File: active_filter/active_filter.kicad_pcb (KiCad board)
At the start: 2 copper layers, 16 parts, among them J1 Screw_Terminal_01x03, J2 Screw_Terminal_01x02, U1 ADA4610-2

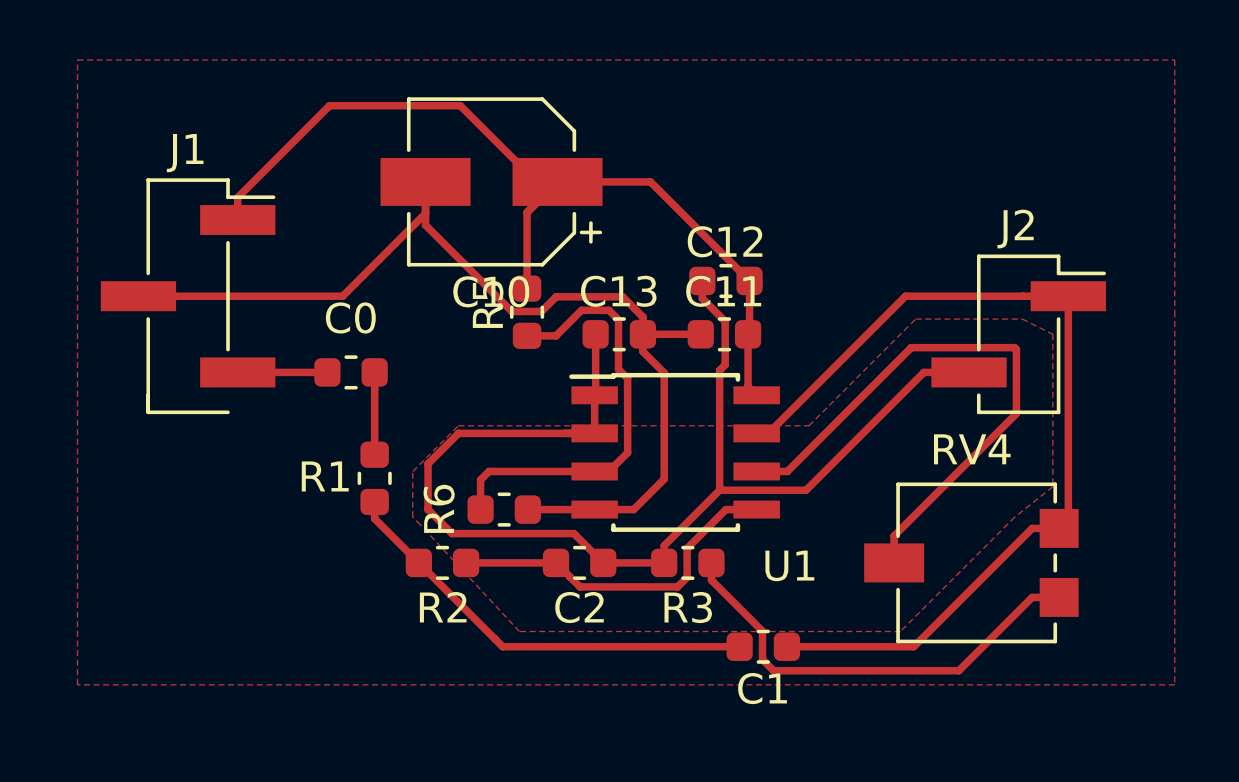
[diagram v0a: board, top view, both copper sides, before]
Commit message: shortened some traces
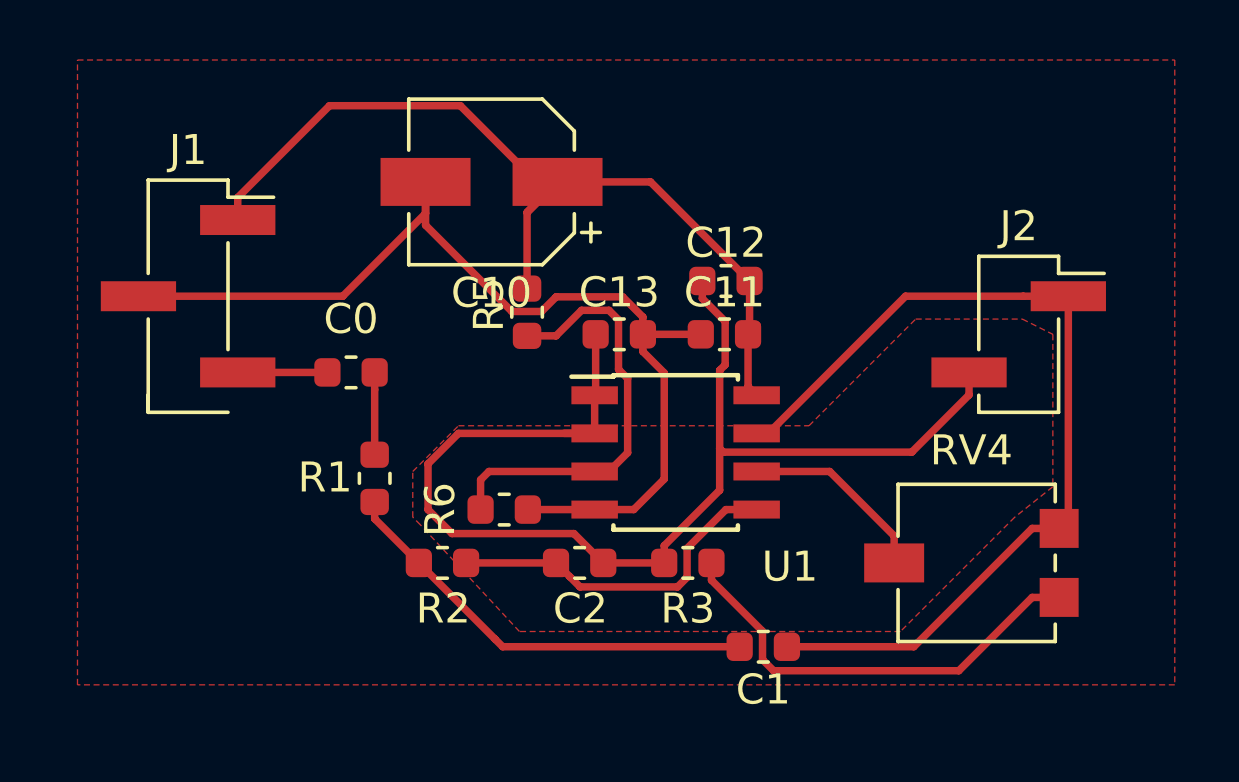
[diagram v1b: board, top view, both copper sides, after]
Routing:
- net Net-(RV4-Pad2): track 19.2 -> 6.37 mm
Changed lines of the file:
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@@
-(kicad_pcb (version 20171130) (host pcbnew 5.0.0)
+(kicad_pcb (version 20171130) (host pcbnew 5.0.0-fee4fd1~66~ubuntu16.04.1)
   (general
     (thickness 1.6)
     (drawings 0)
-    (tracks 107)
+    (tracks 105)
     (zones 0)
     (modules 16)
@@
   (segment (start 30.988 33.782) (end 35.527 33.782) (width 0.25) (layer F.Cu) (net 6))
   (segment (start 29.972 34.798) (end 30.988 33.782) (width 0.25) (layer F.Cu) (net 6))
-  (segment (start 46.501 31.75) (end 48.006 31.75) (width 0.25) (layer F.Cu) (net 6))
-  (segment (start 42.573999 35.677001) (end 46.501 31.75) (width 0.25) (layer F.Cu) (net 6))
-  (segment (start 39.693999 35.677001) (end 42.573999 35.677001) (width 0.25) (layer F.Cu) (net 6))
   (segment (start 37.846 37.525) (end 39.693999 35.677001) (width 0.25) (layer F.Cu) (net 6))
   (segment (start 37.846 38.1) (end 37.846 37.525) (width 0.25) (layer F.Cu) (net 6))
@@
   (segment (start 39.116 28.702) (end 39.116 29.287006) (width 0.25) (layer F.Cu) (net 6))
   (segment (start 39.116 29.287006) (end 39.87749 30.048496) (width 0.25) (layer F.Cu) (net 6))
-  (segment (start 39.693999 31.680001) (end 39.693999 35.677001) (width 0.25) (layer F.Cu) (net 6))
   (segment (start 39.87749 31.49651) (end 39.693999 31.680001) (width 0.25) (layer F.Cu) (net 6))
+  (segment (start 39.811 34.407001) (end 39.693999 34.29) (width 0.25) (layer F.Cu) (net 6))
+  (segment (start 48.006 32.5) (end 46.098999 34.407001) (width 0.25) (layer F.Cu) (net 6))
+  (segment (start 48.006 31.75) (end 48.006 32.5) (width 0.25) (layer F.Cu) (net 6))
+  (segment (start 39.693999 31.680001) (end 39.693999 34.29) (width 0.25) (layer F.Cu) (net 6))
+  (segment (start 46.098999 34.407001) (end 39.811 34.407001) (width 0.25) (layer F.Cu) (net 6))
+  (segment (start 39.693999 34.29) (end 39.693999 35.677001) (width 0.25) (layer F.Cu) (net 6))
   (segment (start 23.63 25.92) (end 26.69 22.86) (width 0.25) (layer F.Cu) (net 7))
   (segment (start 23.63 26.67) (end 23.63 25.92) (width 0.25) (layer F.Cu) (net 7))
@@
   (segment (start 37.135 30.48) (end 39.065 30.48) (width 0.25) (layer F.Cu) (net 8))
   (segment (start 36.002 36.322) (end 35.527 36.322) (width 0.25) (layer F.Cu) (net 8))
-  (segment (start 31.699 36.322) (end 31.496 36.119) (width 0.25) (layer F.Cu) (net 10))
   (segment (start 20.32 29.21) (end 27.13 29.21) (width 0.25) (layer F.Cu) (net 8))
   (segment (start 37.846 31.766) (end 37.135 31.055) (width 0.25) (layer F.Cu) (net 8))
@@
   (segment (start 50.11 39.25) (end 51.01 39.25) (width 0.25) (layer F.Cu) (net 9))
   (segment (start 39.421 38.1) (end 39.421 38.675) (width 0.25) (layer F.Cu) (net 9))
+  (segment (start 31.699 36.322) (end 31.496 36.119) (width 0.25) (layer F.Cu) (net 10))
   (segment (start 31.7245 36.322) (end 31.7245 35.3315) (width 0.25) (layer F.Cu) (net 10))
   (segment (start 32.004 35.052) (end 35.527 35.052) (width 0.25) (layer F.Cu) (net 10))
@@
   (segment (start 34.239 30.531) (end 35.09001 29.67999) (width 0.25) (layer F.Cu) (net 10))
   (segment (start 45.51 37.2) (end 45.51 38.1) (width 0.25) (layer F.Cu) (net 11))
-  (segment (start 49.586001 33.123999) (end 45.51 37.2) (width 0.25) (layer F.Cu) (net 11))
-  (segment (start 49.586001 30.989999) (end 49.586001 33.123999) (width 0.25) (layer F.Cu) (net 11))
-  (segment (start 49.521001 30.924999) (end 49.586001 30.989999) (width 0.25) (layer F.Cu) (net 11))
-  (segment (start 46.079001 30.924999) (end 49.521001 30.924999) (width 0.25) (layer F.Cu) (net 11))
-  (segment (start 41.952 35.052) (end 46.079001 30.924999) (width 0.25) (layer F.Cu) (net 11))
-  (segment (start 40.927 35.052) (end 41.952 35.052) (width 0.25) (layer F.Cu) (net 11))
+  (segment (start 43.362 35.052) (end 45.51 37.2) (width 0.25) (layer F.Cu) (net 11))
+  (segment (start 40.927 35.052) (end 43.362 35.052) (width 0.25) (layer F.Cu) (net 11))
   (zone (net 8) (net_name GND) (layer F.Cu) (hatch edge 0.508)
     (connect_pads (clearance 0.508))

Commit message: added gerber and bom
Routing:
- removed copper zone on F.Cu, net REF
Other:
- board outline added: 36.1 x 21.1 mm
- board text added: "1kHz low-pass"
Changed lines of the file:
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@@
-(kicad_pcb (version 20171130) (host pcbnew 5.0.0-fee4fd1~66~ubuntu16.04.1)
+(kicad_pcb (version 20171130) (host pcbnew 5.0.0)
   (general
     (thickness 1.6)
-    (drawings 0)
+    (drawings 5)
     (tracks 105)
     (zones 0)
@@
   (page A4)
   (layers
-    (0 F.Cu signal)
-    (31 B.Cu signal)
-    (32 B.Adhes user)
-    (33 F.Adhes user)
-    (34 B.Paste user)
-    (35 F.Paste user)
-    (36 B.SilkS user)
+    (0 F.Cu signal hide)
+    (31 B.Cu signal hide)
+    (32 B.Adhes user hide)
+    (33 F.Adhes user hide)
+    (34 B.Paste user hide)
+    (35 F.Paste user hide)
+    (36 B.SilkS user hide)
     (37 F.SilkS user)
-    (38 B.Mask user)
+    (38 B.Mask user hide)
     (39 F.Mask user)
-    (40 Dwgs.User user)
-    (41 Cmts.User user)
-    (42 Eco1.User user)
-    (43 Eco2.User user)
+    (40 Dwgs.User user hide)
+    (41 Cmts.User user hide)
+    (42 Eco1.User user hide)
+    (43 Eco2.User user hide)
     (44 Edge.Cuts user)
     (45 Margin user)
-    (46 B.CrtYd user)
+    (46 B.CrtYd user hide)
     (47 F.CrtYd user)
-    (48 B.Fab user)
-    (49 F.Fab user)
+    (48 B.Fab user hide)
+    (49 F.Fab user hide)
   )
   (setup
@@
     (tags capacitor)
     (attr smd)
-    (fp_text reference C0 (at 0 1.778 180) (layer F.SilkS)
+    (fp_text reference C0 (at -0.0255 1.524 180) (layer F.SilkS)
       (effects (font (size 1 1) (thickness 0.15)))
     )
@@
     (tags "Capacitor Electrolytic")
     (attr smd)
-    (fp_text reference C10 (at 0 -3.7 180) (layer F.SilkS)
+    (fp_text reference C10 (at 5.166 2.032 180) (layer F.SilkS)
       (effects (font (size 1 1) (thickness 0.15)))
     )
@@
     (tags capacitor)
     (attr smd)
-    (fp_text reference C11 (at 0 1.397 180) (layer F.SilkS)
+    (fp_text reference C11 (at -3.0735 0 180) (layer F.SilkS)
       (effects (font (size 1 1) (thickness 0.15)))
     )
@@
     (tags capacitor)
     (attr smd)
-    (fp_text reference C12 (at 0 1.27) (layer F.SilkS)
+    (fp_text reference C12 (at 0.0255 1.524) (layer F.SilkS)
       (effects (font (size 1 1) (thickness 0.15)))
     )
@@
     (tags resistor)
     (attr smd)
-    (fp_text reference R1 (at -0.0255 1.651) (layer F.SilkS)
+    (fp_text reference R1 (at 0.0255 1.778) (layer F.SilkS)
       (effects (font (size 1 1) (thickness 0.15)))
     )
@@
     (tags resistor)
     (attr smd)
-    (fp_text reference R5 (at -0.254 1.27 270) (layer F.SilkS)
+    (fp_text reference R5 (at -0.0255 1.778) (layer F.SilkS)
       (effects (font (size 1 1) (thickness 0.15)))
     )
@@
     (tags resistor)
     (attr smd)
-    (fp_text reference R6 (at -2.1335 0 90) (layer F.SilkS)
+    (fp_text reference R6 (at -0.254 -1.524 180) (layer F.SilkS)
       (effects (font (size 1 1) (thickness 0.15)))
     )
@@
     )
   )
+  (gr_text "1kHz low-pass" (at 44.958 23.622) (layer F.Cu)
+    (effects (font (size 1.5 1.5) (thickness 0.3)))
+  )
+  (gr_line (start 17.78 42.926) (end 17.78 21.844) (layer Edge.Cuts) (width 0.15))
+  (gr_line (start 53.848 42.926) (end 17.78 42.926) (layer Edge.Cuts) (width 0.15))
+  (gr_line (start 53.848 21.844) (end 53.848 42.926) (layer Edge.Cuts) (width 0.15))
+  (gr_line (start 17.78 21.844) (end 53.848 21.844) (layer Edge.Cuts) (width 0.15))
   (segment (start 23.63 31.75) (end 26.619 31.75) (width 0.25) (layer F.Cu) (net 1))
   (segment (start 28.194 32.325) (end 28.194 34.493) (width 0.25) (layer F.Cu) (net 2))
@@
     (polygon
       (pts
-        (xy 54.864 42.164) (xy 18.288 42.164) (xy 18.288 21.336) (xy 54.864 21.336) (xy 54.864 29.718)
+        (xy 17.78 21.844) (xy 53.848 21.844) (xy 53.848 42.926) (xy 17.78 42.926)
       )
     )
-  )
-  (zone (net 6) (net_name REF) (layer F.Cu) (hatch edge 0.508)
-    (connect_pads (clearance 0.508))
-    (min_thickness 0.254)
-    (fill yes (arc_segments 16) (thermal_gap 0.508) (thermal_bridge_width 0.508))
-    (polygon
-      (pts
-        (xy 49.53 36.576) (xy 45.72 40.386) (xy 33.02 40.386) (xy 29.718 36.83) (xy 29.464 36.576)
-        (xy 29.464 35.052) (xy 30.988 33.528) (xy 42.672 33.528) (xy 46.228 29.972) (xy 49.784 29.972)
-        (xy 50.8 30.48) (xy 50.8 35.56)
-      )
-    )

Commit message: SYNC:
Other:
- board text added: "1kHz Tiefpass"
- board text removed: "1kHz low-pass"
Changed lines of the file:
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@@
   (page A4)
   (layers
-    (0 F.Cu signal hide)
+    (0 F.Cu signal)
     (31 B.Cu signal hide)
     (32 B.Adhes user hide)
@@
     (visible_elements FFFFFF7F)
     (pcbplotparams
-      (layerselection 0x010fc_ffffffff)
+      (layerselection 0x010a0_7fffffff)
       (usegerberextensions false)
       (usegerberattributes false)
@@
       (padsonsilk false)
       (subtractmaskfromsilk false)
-      (outputformat 1)
+      (outputformat 5)
       (mirror false)
-      (drillshape 1)
+      (drillshape 0)
       (scaleselection 1)
       (outputdirectory ""))
@@
     )
   )
-  (gr_text "1kHz low-pass" (at 44.958 23.622) (layer F.Cu)
+  (gr_text "1kHz Tiefpass" (at 44.958 23.622) (layer F.Cu)
     (effects (font (size 1.5 1.5) (thickness 0.3)))
   )

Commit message: added simulation
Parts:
- removed C0: 100n, default-footprints:C_0603_1608Metric
- C1: value 1.2n -> 2.2n
- C2: value 1.2n -> 220p
- R1: value 18k -> 47k
- U1: value ADA4610-2 -> ADA4062-2
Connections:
- R1 pad 1: Net-(C0-Pad1) -> IN
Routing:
- net Net-(C0-Pad1): track 2.74 -> 0.00 mm
- net IN: track 2.99 -> 5.70 mm
